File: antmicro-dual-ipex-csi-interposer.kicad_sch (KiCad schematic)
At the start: 18 parts, among them J1 WE_68715014522, J2 MSAK24025P30

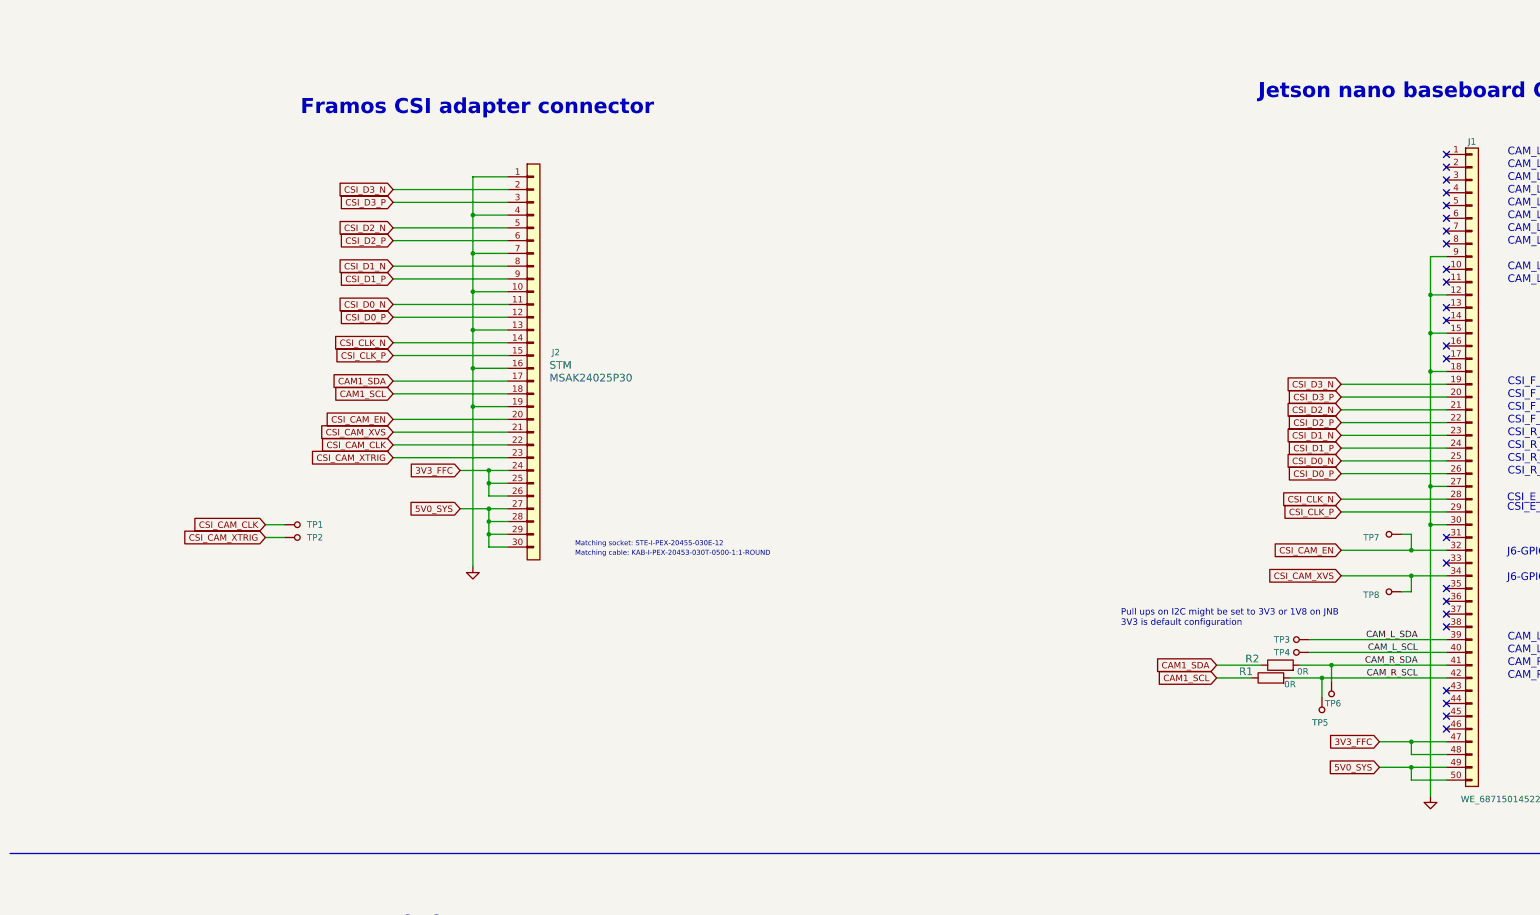
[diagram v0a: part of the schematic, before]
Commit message: Add second connector and assigned signals
Remove Kicad5 CI
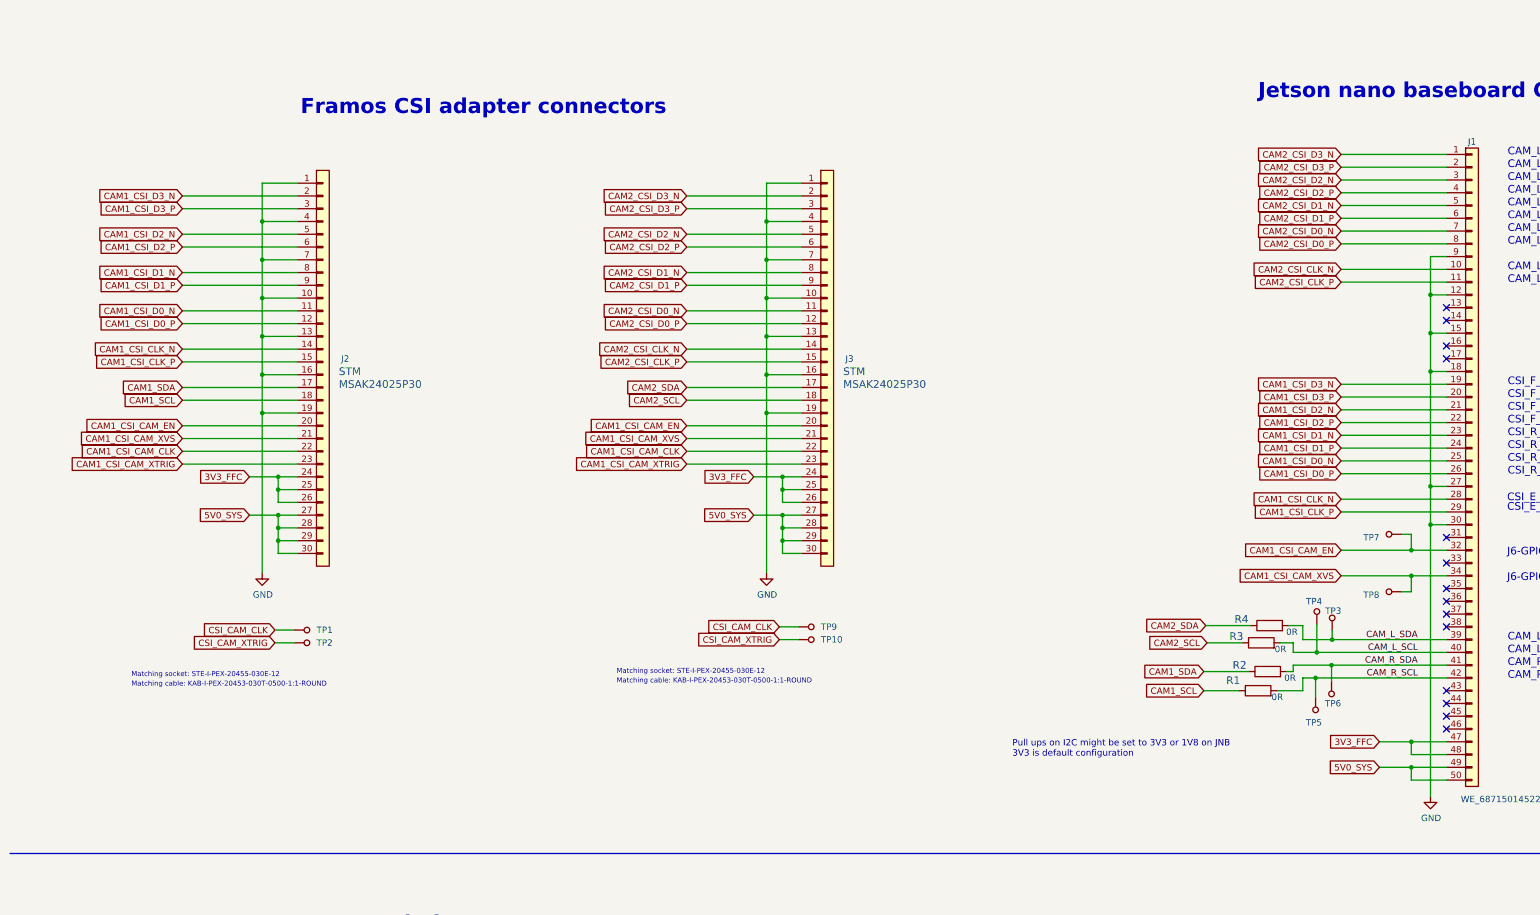
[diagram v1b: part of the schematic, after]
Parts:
- added J3: MSAK24025P30, antmicro-footprints:MSAK24025P30, symbol antmicroFCCConnectors:MSAK24025P30
- added R3, R4: R_0R_0402, antmicro-footprints:0402-res, symbol antmicroResistors0402:R_0R_0402
- added TP10, TP9: TP_SMD1MM, antmicro-footprints:Testpoint_smd_1mm, symbol antmicroTestPoints:TP_SMD1MM
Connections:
- net 3V3_FFC: now also J3.24 (Pin_24), J3.25 (Pin_25), J3.26 (Pin_26)
- net 5V0_SYS: now also J3.27 (Pin_27), J3.28 (Pin_28), J3.29 (Pin_29), J3.30 (Pin_30)
- net CAM_L_SCL: now also R3.2
- net CAM_L_SDA: now also R4.2
- net CSI_CAM_CLK: now also TP9.1; no longer J2.22 (Pin_22)
- net CSI_CAM_XTRIG: now also TP10.1; no longer J2.23 (Pin_23)
- net GND: now also J3.1 (Pin_1), J3.10 (Pin_10), J3.13 (Pin_13), J3.16 (Pin_16), J3.19 (Pin_19), J3.4 (Pin_4), J3.7 (Pin_7)
- net CAM2_CSI_D3_N: now reaches J1.1 (Pin_1)
- net CAM2_CSI_D3_N: now also J3.2 (Pin_2)
- net CAM2_CSI_CLK_N: now reaches J1.10 (Pin_10)
- net CAM2_CSI_CLK_N: now also J3.14 (Pin_14)
- net CAM2_CSI_CLK_P: now reaches J1.11 (Pin_11)
- net CAM2_CSI_CLK_P: now also J3.15 (Pin_15)
- net CAM2_CSI_D3_P: now reaches J1.2 (Pin_2)
- net CAM2_CSI_D3_P: now also J3.3 (Pin_3)
- net CAM2_CSI_D2_N: now reaches J1.3 (Pin_3)
- net CAM2_CSI_D2_N: now also J3.5 (Pin_5)
- net CAM2_CSI_D2_P: now reaches J1.4 (Pin_4)
- net CAM2_CSI_D2_P: now also J3.6 (Pin_6)
- net CAM2_CSI_D1_N: now reaches J1.5 (Pin_5)
- net CAM2_CSI_D1_N: now also J3.8 (Pin_8)
- net CAM2_CSI_D1_P: now reaches J1.6 (Pin_6)
- net CAM2_CSI_D1_P: now also J3.9 (Pin_9)
- net CAM2_CSI_D0_N: now reaches J1.7 (Pin_7)
- net CAM2_CSI_D0_N: now also J3.11 (Pin_11)
- net CAM2_CSI_D0_P: now reaches J1.8 (Pin_8)
- net CAM2_CSI_D0_P: now also J3.12 (Pin_12)
- net CSI_CAM_EN renamed CAM1_CSI_CAM_EN
- net CAM1_CSI_CAM_EN: now also J3.20 (Pin_20)
- net CSI_CAM_XVS renamed CAM1_CSI_CAM_XVS
- net CAM1_CSI_CAM_XVS: now also J3.21 (Pin_21)
- net CSI_CLK_N renamed CAM1_CSI_CLK_N
- net CSI_CLK_P renamed CAM1_CSI_CLK_P
- net CSI_D0_N renamed CAM1_CSI_D0_N
- net CSI_D0_P renamed CAM1_CSI_D0_P
- net CSI_D1_N renamed CAM1_CSI_D1_N
- net CSI_D1_P renamed CAM1_CSI_D1_P
- net CSI_D2_N renamed CAM1_CSI_D2_N
- net CSI_D2_P renamed CAM1_CSI_D2_P
- net CSI_D3_N renamed CAM1_CSI_D3_N
- net CSI_D3_P renamed CAM1_CSI_D3_P
- new net CAM1_CSI_CAM_CLK: J2.22 (Pin_22), J3.22 (Pin_22)
- new net CAM1_CSI_CAM_XTRIG: J2.23 (Pin_23), J3.23 (Pin_23)
- new net CAM2_SCL: J3.18 (Pin_18), R3.1
- new net CAM2_SDA: J3.17 (Pin_17), R4.1
- no-connect marks 24 -> 14
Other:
- note added: "Framos CSI adapter connectors"
- note removed: "Framos CSI adapter connector"
- moved on the sheet: J2, R1, R2, TP1, TP2, TP3, TP4, TP5

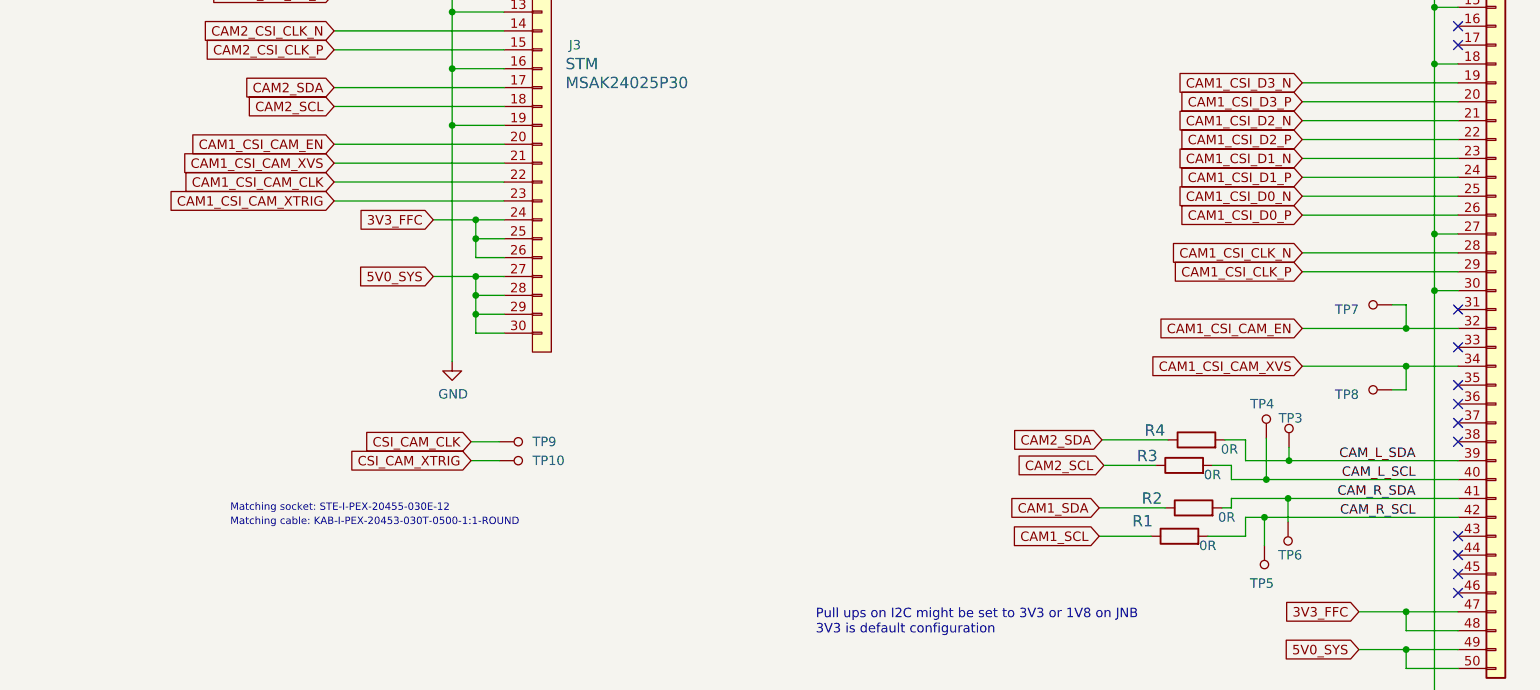
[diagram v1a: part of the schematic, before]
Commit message: Complete schematic. Proceed PCB layout
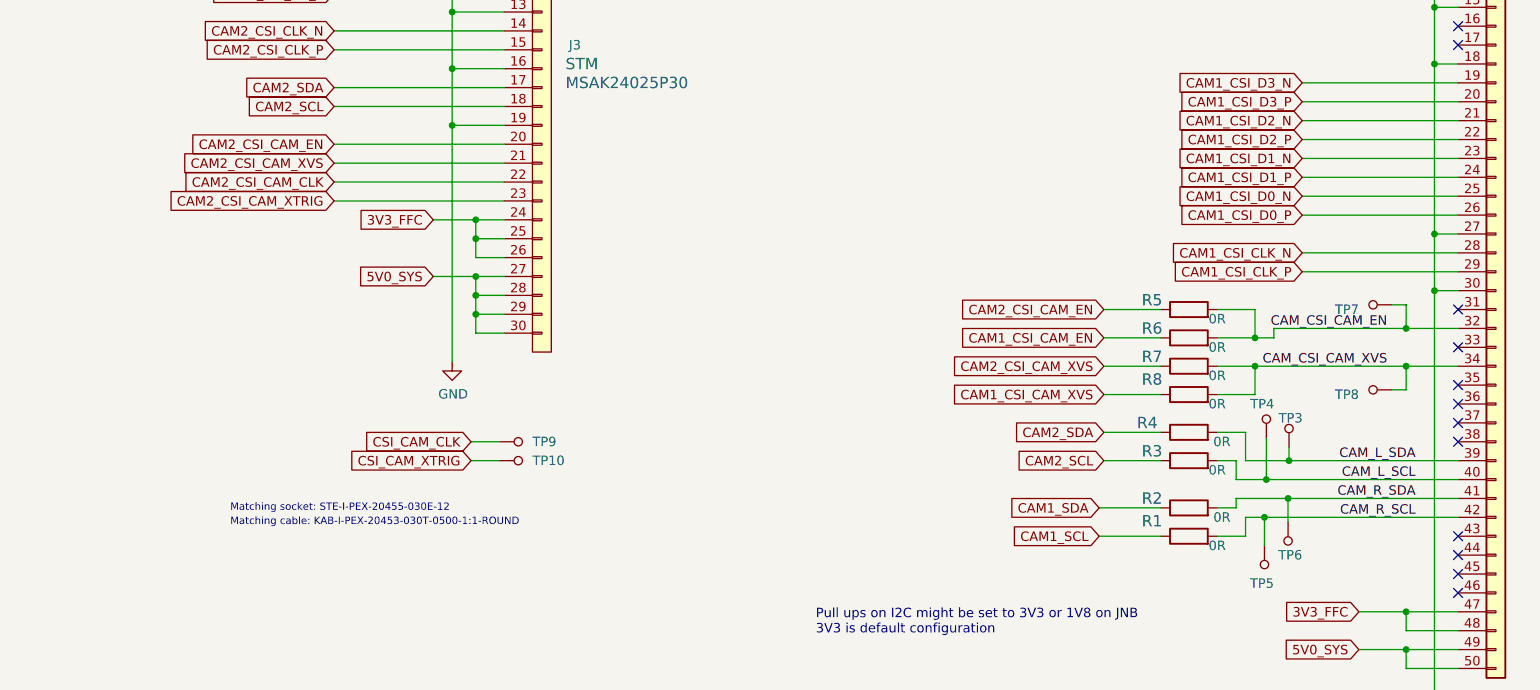
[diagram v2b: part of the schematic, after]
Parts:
- added R5, R6, R7, R8: R_0R_0402, antmicro-footprints:0402-res, symbol antmicroResistors0402:R_0R_0402
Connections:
- net CAM1_CSI_CAM_CLK: no longer J3.22 (Pin_22)
- net CAM1_CSI_CAM_EN: now also R6.1; no longer J1.32 (Pin_32), J3.20 (Pin_20), TP7.1
- net CAM1_CSI_CAM_XTRIG: no longer J3.23 (Pin_23)
- net CAM1_CSI_CAM_XVS: now also R8.1; no longer J1.34 (Pin_34), J3.21 (Pin_21), TP8.1
- new net CAM2_CSI_CAM_CLK: J3.22 (Pin_22)
- new net CAM2_CSI_CAM_EN: J3.20 (Pin_20), R5.1
- new net CAM2_CSI_CAM_XTRIG: J3.23 (Pin_23)
- new net CAM2_CSI_CAM_XVS: J3.21 (Pin_21), R7.1
- new net CAM_CSI_CAM_EN: J1.32 (Pin_32), R5.2, R6.2, TP7.1
- new net CAM_CSI_CAM_XVS: J1.34 (Pin_34), R7.2, R8.2, TP8.1
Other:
- moved on the sheet: R1, R2, R3, R4

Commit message: Route low speed, optimize polygons, match lane length
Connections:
- net CAM1_CSI_CAM_CLK: now also TP1.1
- net CAM1_CSI_CAM_XTRIG: now also TP2.1
- net CAM2_CSI_CAM_CLK: now also TP9.1
- net CAM2_CSI_CAM_XTRIG: now also TP10.1
- removed net CSI_CAM_CLK: TP1.1, TP9.1
- removed net CSI_CAM_XTRIG: TP10.1, TP2.1
- no-connect marks 14 -> 18
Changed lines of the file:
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@@
   (no_connect (at 297.815 172.72))
   (no_connect (at 297.815 99.06))
+  (no_connect (at 88.9 91.44))
   (no_connect (at 297.815 96.52))
   (no_connect (at 297.815 160.02))
@@
   (no_connect (at 297.815 106.68))
   (no_connect (at 297.815 180.34))
+  (no_connect (at 194.31 91.44))
+  (no_connect (at -48.26 85.09))
+  (no_connect (at 412.75 68.58))
   (no_connect (at 297.815 142.24))
   (no_connect (at 297.815 154.94))
@@
     )
   )
-  (global_label "CSI_CAM_XTRIG" (shape input) (at 64.77 163.195 180) (fields_autoplaced)
-    (effects (font (size 1.27 1.27)) (justify right))
-    (property "Intersheet References" "${INTERSHEET_REFS}" (id 0) (at 1.905 20.955 0)
-      (effects (font (size 1.27 1.27)) hide)
+  (global_label "CAM1_CSI_CAM_XTRIG" (shape input) (at 64.77 163.195 180) (fields_autoplaced)
+    (effects (font (size 1.27 1.27)) (justify right))
+    (property "Intersheet References" "${INTERSHEET_REFS}" (id 0) (at 42.3072 163.1156 0)
+      (effects (font (size 1.27 1.27)) (justify right) hide)
     )
   )
@@
     )
   )
-  (global_label "CSI_CAM_CLK" (shape input) (at 165.1 160.02 180) (fields_autoplaced)
-    (effects (font (size 1.27 1.27)) (justify right))
-    (property "Intersheet References" "${INTERSHEET_REFS}" (id 0) (at 102.235 20.32 0)
-      (effects (font (size 1.27 1.27)) hide)
+  (global_label "CAM2_CSI_CAM_CLK" (shape input) (at 165.1 160.02 180) (fields_autoplaced)
+    (effects (font (size 1.27 1.27)) (justify right))
+    (property "Intersheet References" "${INTERSHEET_REFS}" (id 0) (at 144.391 159.9406 0)
+      (effects (font (size 1.27 1.27)) (justify right) hide)
     )
   )
@@
     )
   )
-  (global_label "CSI_CAM_CLK" (shape input) (at 64.77 160.655 180) (fields_autoplaced)
-    (effects (font (size 1.27 1.27)) (justify right))
-    (property "Intersheet References" "${INTERSHEET_REFS}" (id 0) (at 1.905 20.955 0)
-      (effects (font (size 1.27 1.27)) hide)
+  (global_label "CAM1_CSI_CAM_CLK" (shape input) (at 64.77 160.655 180) (fields_autoplaced)
+    (effects (font (size 1.27 1.27)) (justify right))
+    (property "Intersheet References" "${INTERSHEET_REFS}" (id 0) (at 44.061 160.5756 0)
+      (effects (font (size 1.27 1.27)) (justify right) hide)
     )
   )
@@
     )
   )
-  (global_label "CSI_CAM_XTRIG" (shape input) (at 165.1 162.56 180) (fields_autoplaced)
-    (effects (font (size 1.27 1.27)) (justify right))
-    (property "Intersheet References" "${INTERSHEET_REFS}" (id 0) (at 102.235 20.32 0)
-      (effects (font (size 1.27 1.27)) hide)
-    )
-  )
+  (global_label "CAM2_CSI_CAM_XTRIG" (shape input) (at 165.1 162.56 180) (fields_autoplaced)
+    (effects (font (size 1.27 1.27)) (justify right))
+    (property "Intersheet References" "${INTERSHEET_REFS}" (id 0) (at 142.6372 162.4806 0)
+      (effects (font (size 1.27 1.27)) (justify right) hide)
+    )
+  )
